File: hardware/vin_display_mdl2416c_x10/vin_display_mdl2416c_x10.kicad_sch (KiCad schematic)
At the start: 34 parts

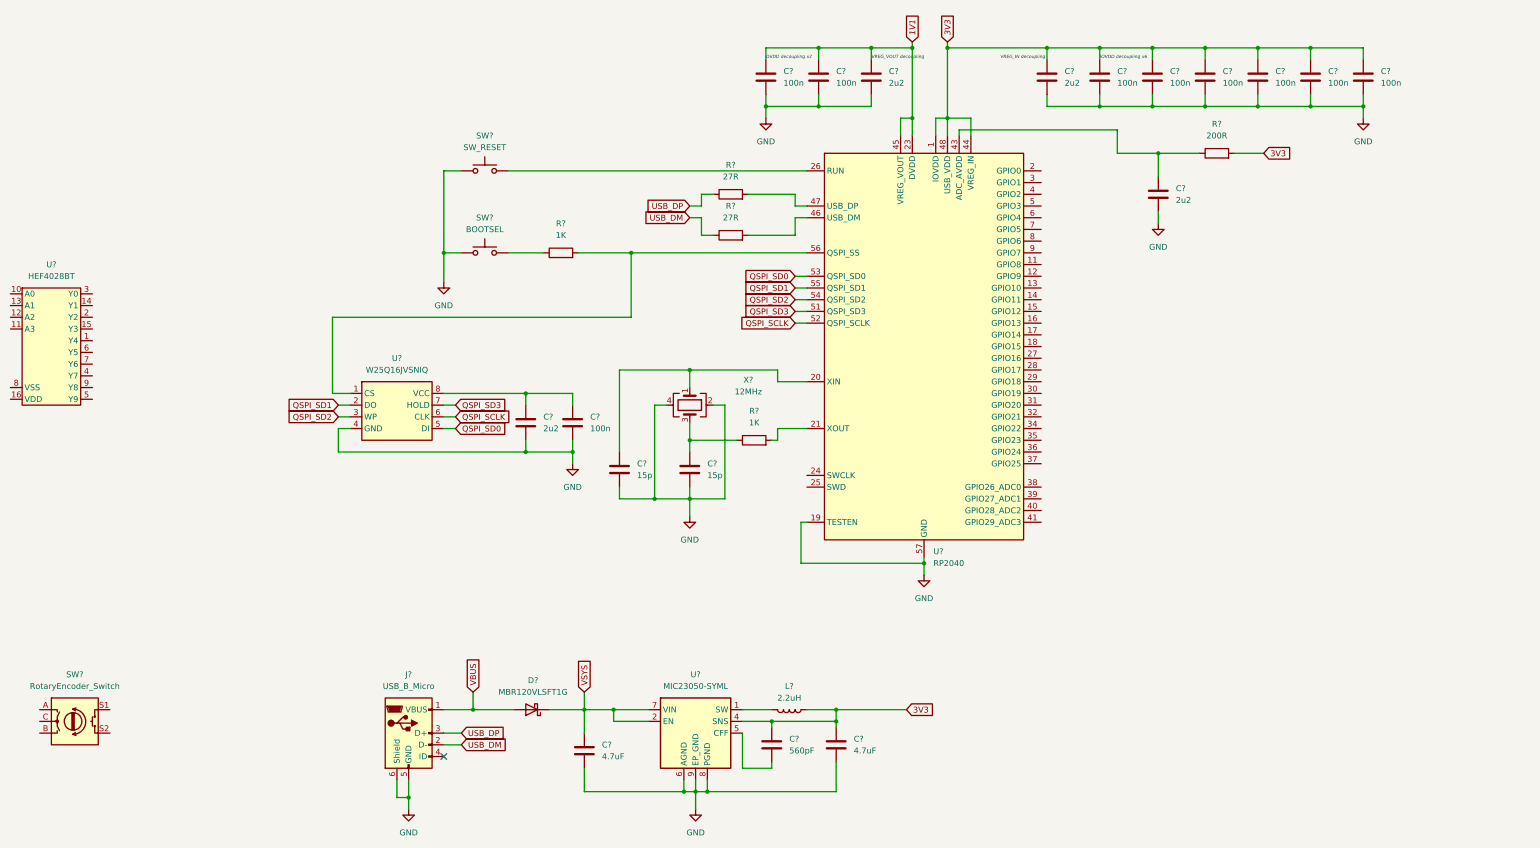
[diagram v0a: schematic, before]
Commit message: complete mdl2416c display schematics
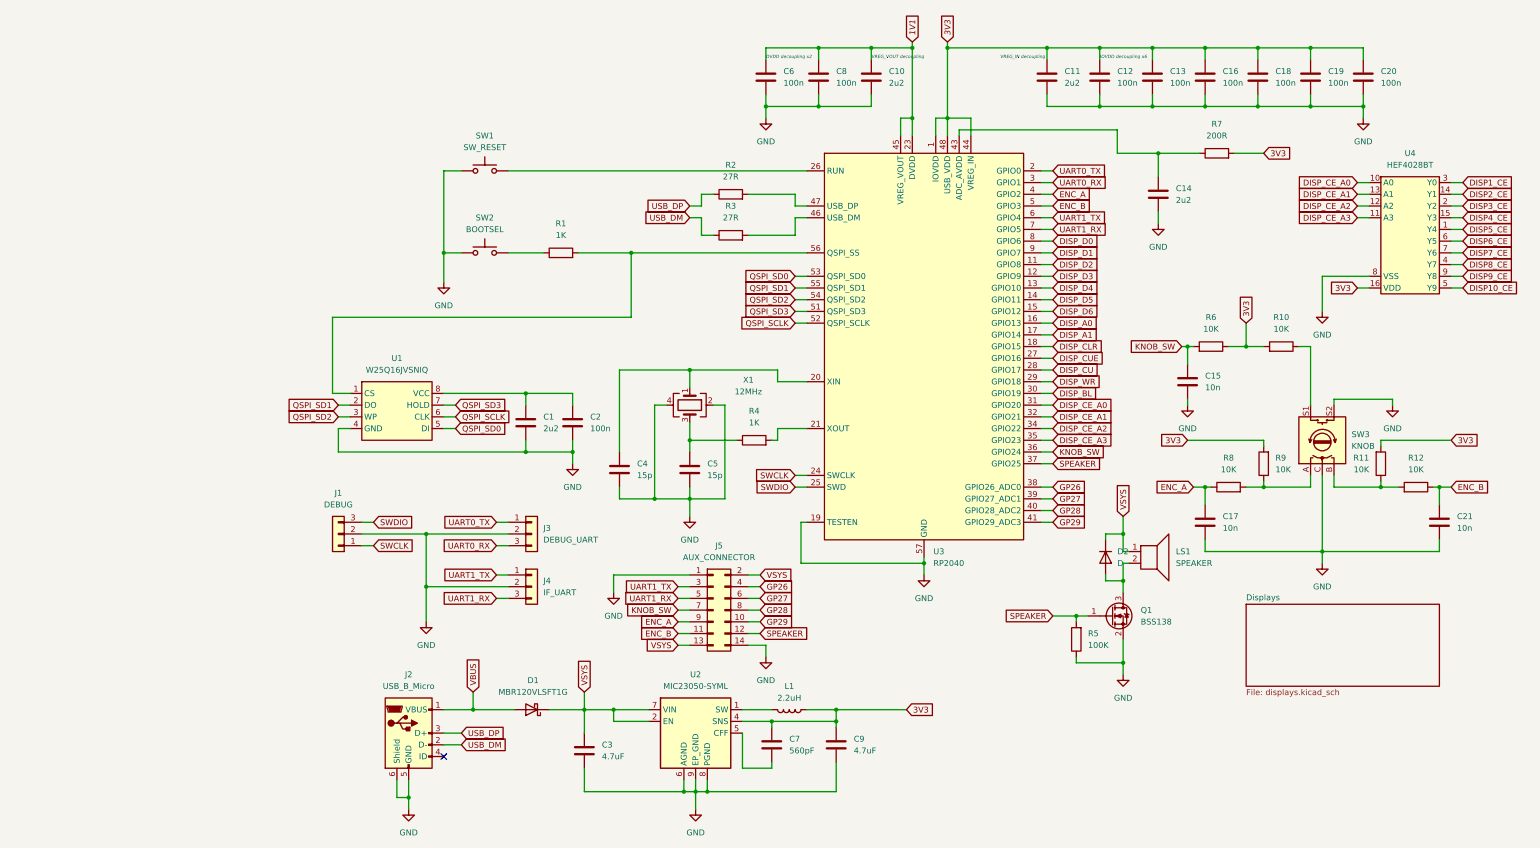
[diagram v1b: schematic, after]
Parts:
- added C15, C17, C21: 10n, symbol Device:C
- added D2: D, symbol Device:D
- added J1: DEBUG, symbol Connector_Generic:Conn_01x03
- added J3: DEBUG_UART, symbol Connector_Generic:Conn_01x03
- added J4: IF_UART, symbol Connector_Generic:Conn_01x03
- added J5: AUX_CONNECTOR, symbol Connector_Generic:Conn_02x07_Odd_Even
- added LS1: SPEAKER, symbol Device:Speaker
- added Q1: BSS138, Package_TO_SOT_SMD:SOT-23, symbol Transistor_FET:BSS138
- added R10, R11, R12, R6, R8, R9: 10K, symbol Device:R
- added R5: 100K, symbol Device:R
- SW3: renamed from SW?; value RotaryEncoder_Switch -> KNOB
- gave numbers to parts that had none: 33
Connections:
- net 3V3: now also U4.16 (VDD), R10.2, R11.2, R6.1, R9.2
- net GND: now also SW3.C, SW3.S2, U4.8 (VSS), C15.2, C17.2, C21.2, J1.2 (Pin_2), J3.2 (Pin_2), J4.2 (Pin_2), J5.1 (Pin_1), J5.14 (Pin_14), Q1.2 (S), R5.1
- net VSYS: now also D2.1 (K), J5.13 (Pin_13), J5.2 (Pin_2), LS1.1
- net DISP5_CE: now reaches U4.1 (Y4)
- net DISP_CE_A0: now reaches U4.10 (A0)
- net DISP_CE_A0: now also U3.31 (GPIO20)
- net DISP_CE_A3: now reaches U4.11 (A3)
- net DISP_CE_A3: now also U3.35 (GPIO23)
- net DISP_CE_A2: now reaches U4.12 (A2)
- net DISP_CE_A2: now also U3.34 (GPIO22)
- net DISP_CE_A1: now reaches U4.13 (A1)
- net DISP_CE_A1: now also U3.32 (GPIO21)
- net DISP2_CE: now reaches U4.14 (Y1)
- net DISP4_CE: now reaches U4.15 (Y3)
- net DISP3_CE: now reaches U4.2 (Y2)
- net DISP1_CE: now reaches U4.3 (Y0)
- net DISP8_CE: now reaches U4.4 (Y7)
- net DISP10_CE: now reaches U4.5 (Y9)
- net DISP6_CE: now reaches U4.6 (Y5)
- net DISP7_CE: now reaches U4.7 (Y6)
- net DISP9_CE: now reaches U4.9 (Y8)
- net DISP_D2: now reaches U3.11 (GPIO8)
- net DISP_D3: now reaches U3.12 (GPIO9)
- net DISP_D4: now reaches U3.13 (GPIO10)
- net DISP_D5: now reaches U3.14 (GPIO11)
- net DISP_D6: now reaches U3.15 (GPIO12)
- net DISP_A0: now reaches U3.16 (GPIO13)
- net DISP_A1: now reaches U3.17 (GPIO14)
- net DISP_CLR: now reaches U3.18 (GPIO15)
- net UART0_TX: now reaches U3.2 (GPIO0)
- net UART0_TX: now also J3.1 (Pin_1)
- net SWCLK: now reaches U3.24 (SWCLK)
- net SWCLK: now also J1.1 (Pin_1)
- net SWDIO: now reaches U3.25 (SWD)
- net SWDIO: now also J1.3 (Pin_3)
- net DISP_CUE: now reaches U3.27 (GPIO16)
- net DISP_CU: now reaches U3.28 (GPIO17)
- net DISP_WR: now reaches U3.29 (GPIO18)
- net UART0_RX: now reaches U3.3 (GPIO1)
- net UART0_RX: now also J3.3 (Pin_3)
- net DISP_BL: now reaches U3.30 (GPIO19)
- net KNOB_SW: now reaches U3.36 (GPIO24)
- net KNOB_SW: now also C15.1, J5.7 (Pin_7), R6.2
- net SPEAKER: now reaches U3.37 (GPIO25)
- net SPEAKER: now also J5.12 (Pin_12), Q1.1 (G), R5.2
- net GP26: now reaches U3.38 (GPIO26_ADC0)
- net GP26: now also J5.4 (Pin_4)
- net GP27: now reaches U3.39 (GPIO27_ADC1)
- net GP27: now also J5.6 (Pin_6)
- net ENC_A: now reaches U3.4 (GPIO2)
- net ENC_A: now also C17.1, J5.9 (Pin_9), R8.1
- net GP28: now reaches U3.40 (GPIO28_ADC2)
- net GP28: now also J5.8 (Pin_8)
- net GP29: now reaches U3.41 (GPIO29_ADC3)
- net GP29: now also J5.10 (Pin_10)
- net ENC_B: now reaches U3.5 (GPIO3)
- net ENC_B: now also C21.1, J5.11 (Pin_11), R12.1
- net UART1_TX: now reaches U3.6 (GPIO4)
- net UART1_TX: now also J4.1 (Pin_1), J5.3 (Pin_3)
- net UART1_RX: now reaches U3.7 (GPIO5)
- net UART1_RX: now also J4.3 (Pin_3), J5.5 (Pin_5)
- net DISP_D0: now reaches U3.8 (GPIO6)
- net DISP_D1: now reaches U3.9 (GPIO7)
- net at SW3.A: now also R8.2, R9.1
- net at SW3.B: now also R11.1, R12.2
- net at SW3.S1: now also R10.1
- new net: D2.2 (A), LS1.2, Q1.3 (D)
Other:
- added sheet Displays (displays.kicad_sch)
- moved on the sheet: SW3, U4

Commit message: assign component footprints; basic pcb layout
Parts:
- C1, C10, C11, C12, C13, C14, C15, C16, C17, C18, C19, C2, C20, C21, C3, C4, C5, C6, C7, C8, C9: footprint (none) -> Capacitor_SMD:C_0603_1608Metric
- D1: value MBR120VLSFT1G -> MBR1020VL; footprint (none) -> Diode_SMD:D_SOD-123F
- D2: footprint (none) -> Diode_SMD:D_SOD-123
- J1, J3, J4: footprint (none) -> Connector_PinHeader_2.54mm:PinHeader_1x03_P2.54mm_Vertical
- J2: footprint (none) -> components:GCT_USB3140
- J5: footprint (none) -> Connector_IDC:IDC-Header_2x07_P2.54mm_Vertical
- L1: footprint (none) -> components:Inductor_0806
- LS1: footprint (none) -> components:BUZZER_CMT-8504
- R1, R10, R11, R12, R2, R3, R4, R5, R6, R7, R8, R9: footprint (none) -> Resistor_SMD:R_0603_1608Metric
- SW1, SW2: footprint (none) -> components:TS18_TACTILE_SWITCH
- SW3: footprint (none) -> components:PEC11H_Encoder
- X1: footprint (none) -> Crystal:Crystal_SMD_Abracon_ABM8AIG-4Pin_3.2x2.5mm

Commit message: work on pcb layout
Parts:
- removed J4: IF_UART, Connector_PinHeader_2.54mm:PinHeader_1x03_P2.54mm_Vertical, symbol Connector_Generic:Conn_01x03
- added J4: Conn_01x04, Connector_PinHeader_2.54mm:PinHeader_1x04_P2.54mm_Vertical, symbol Connector_Generic:Conn_01x04
- U2: footprint Package_DFN_QFN:Micrel_MLF-8-1EP_2x2mm_P0.5mm_EP0.6x1.2mm_ThermalVias -> Package_DFN_QFN:Micrel_MLF-8-1EP_2x2mm_P0.5mm_EP0.6x1.2mm
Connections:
- net 3V3: now also C1.1, C2.1, U1.8 (VCC)
- net GND: now also J4.3 (Pin_3)
- net UART1_RX: now also J4.4 (Pin_4)
- net UART1_TX: now also J4.2 (Pin_2)
- net VSYS: now also J4.1 (Pin_1)
- net USB_D-: now reaches R3.2, U3.46 (USB_DM)
- net USB_D+: now reaches R2.2, U3.47 (USB_DP)
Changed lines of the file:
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@@
+    (stroke (width 0) (type default) (color 0 0 0 0))
+  )
+  (wire (pts (xy 60.96 134.62) (xy 63.5 134.62))
     (stroke (width 0) (type default) (color 0 0 0 0))
   )
@@
     )
   )
+  (global_label "3V3" (shape input) (at 67.31 97.79 90) (fields_autoplaced)
+    (effects (font (size 1.27 1.27)) (justify left))
+    (property "Intersheet References" "${INTERSHEET_REFS}" (id 0) (at 67.2306 91.8693 90)
+      (effects (font (size 1.27 1.27)) (justify left) hide)
+    )
+  )
   (global_label "VBUS" (shape input) (at 55.88 162.56 90) (fields_autoplaced)
     (effects (font (size 1.27 1.27)) (justify left))
@@
     (property "Intersheet References" "${INTERSHEET_REFS}" (id 0) (at 193.0341 59.6106 0)
       (effects (font (size 1.27 1.27)) (justify left) hide)
+    )
+  )
+  (global_label "USB_D-" (shape input) (at 125.73 59.69 180) (fields_autoplaced)
+    (effects (font (size 1.27 1.27)) (justify right))
+    (property "Intersheet References" "${INTERSHEET_REFS}" (id 0) (at 115.6969 59.6106 0)
+      (effects (font (size 1.27 1.27)) (justify right) hide)
     )
   )
@@
     (effects (font (size 1.27 1.27)) (justify right))
     (property "Intersheet References" "${INTERSHEET_REFS}" (id 0) (at 114.2455 72.4694 0)
+      (effects (font (size 1.27 1.27)) (justify right) hide)
+    )
+  )
+  (global_label "USB_D+" (shape input) (at 125.73 57.15 180) (fields_autoplaced)
+    (effects (font (size 1.27 1.27)) (justify right))
+    (property "Intersheet References" "${INTERSHEET_REFS}" (id 0) (at 115.6969 57.0706 0)
+      (effects (font (size 1.27 1.27)) (justify right) hide)
+    )
+  )
+  (global_label "VSYS" (shape input) (at 60.96 134.62 180) (fields_autoplaced)
+    (effects (font (size 1.27 1.27)) (justify right))
+    (property "Intersheet References" "${INTERSHEET_REFS}" (id 0) (at 53.9507 134.5406 0)
       (effects (font (size 1.27 1.27)) (justify right) hide)
     )
@@
     )
     (property "Datasheet" "~" (id 3) (at 26.67 128.27 0)
-      (effects (font (size 1.27 1.27)) hide)
-    )
-    (pin "1")
-    (pin "2")
-    (pin "3")
-  )
-  (symbol (lib_id "Connector_Generic:Conn_01x03") (at 68.58 139.7 0) (unit 1)
-    (in_bom yes) (on_board yes) (fields_autoplaced)
-    (property "Reference" "J4" (id 0) (at 71.12 138.4299 0)
-      (effects (font (size 1.27 1.27)) (justify left))
-    )
-    (property "Value" "IF_UART" (id 1) (at 71.12 140.9699 0)
-      (effects (font (size 1.27 1.27)) (justify left))
-    )
-    (property "Footprint" "Connector_PinHeader_2.54mm:PinHeader_1x03_P2.54mm_Vertical" (id 2) (at 68.58 139.7 0)
-      (effects (font (size 1.27 1.27)) hide)
-    )
-    (property "Datasheet" "~" (id 3) (at 68.58 139.7 0)
       (effects (font (size 1.27 1.27)) hide)
     )
@@
     (pin "2")
   )
+  (symbol (lib_id "Connector_Generic:Conn_01x04") (at 68.58 137.16 0) (unit 1)
+    (in_bom yes) (on_board yes) (fields_autoplaced)
+    (property "Reference" "J4" (id 0) (at 71.12 137.1599 0)
+      (effects (font (size 1.27 1.27)) (justify left))
+    )
+    (property "Value" "Conn_01x04" (id 1) (at 71.12 139.6999 0)
+      (effects (font (size 1.27 1.27)) (justify left))
+    )
+    (property "Footprint" "Connector_PinHeader_2.54mm:PinHeader_1x04_P2.54mm_Vertical" (id 2) (at 68.58 137.16 0)
+      (effects (font (size 1.27 1.27)) hide)
+    )
+    (property "Datasheet" "~" (id 3) (at 68.58 137.16 0)
+      (effects (font (size 1.27 1.27)) hide)
+    )
+    (pin "1")
+    (pin "2")
+    (pin "3")
+    (pin "4")
+  )
   (symbol (lib_id "Device:R") (at 111.76 54.61 90) (unit 1)
     (in_bom yes) (on_board yes) (fields_autoplaced)
@@
     (property "Reference" "U2" (id 0) (at 104.14 158.75 0))
     (property "Value" "MIC23050-SYML" (id 1) (at 104.14 161.29 0))
-    (property "Footprint" "Package_DFN_QFN:Micrel_MLF-8-1EP_2x2mm_P0.5mm_EP0.6x1.2mm_ThermalVias" (id 2) (at 109.22 170.18 0)
+    (property "Footprint" "Package_DFN_QFN:Micrel_MLF-8-1EP_2x2mm_P0.5mm_EP0.6x1.2mm" (id 2) (at 109.22 170.18 0)
       (effects (font (size 1.27 1.27)) (justify left) hide)
     )
@@
       (reference "J3") (unit 1) (value "DEBUG_UART") (footprint "Connector_PinHeader_2.54mm:PinHeader_1x03_P2.54mm_Vertical")
     )
-    (path "/52948f66-709e-42ba-95a6-a598f591e63a"
-      (reference "J4") (unit 1) (value "IF_UART") (footprint "Connector_PinHeader_2.54mm:PinHeader_1x03_P2.54mm_Vertical")
+    (path "/83b99386-65f3-4d5f-ace0-dfc7848335c3"
+      (reference "J4") (unit 1) (value "Conn_01x04") (footprint "Connector_PinHeader_2.54mm:PinHeader_1x04_P2.54mm_Vertical")
     )
     (path "/24dea3f5-faa1-4f14-a163-ea0dcc26d440"
@@
     )
     (path "/fc845537-7277-43cf-9d22-ef1876c41284"
-      (reference "U2") (unit 1) (value "MIC23050-SYML") (footprint "Package_DFN_QFN:Micrel_MLF-8-1EP_2x2mm_P0.5mm_EP0.6x1.2mm_ThermalVias")
+      (reference "U2") (unit 1) (value "MIC23050-SYML") (footprint "Package_DFN_QFN:Micrel_MLF-8-1EP_2x2mm_P0.5mm_EP0.6x1.2mm")
     )
     (path "/73b74445-0b4c-42ed-8ac5-ea72e30c4bc1"

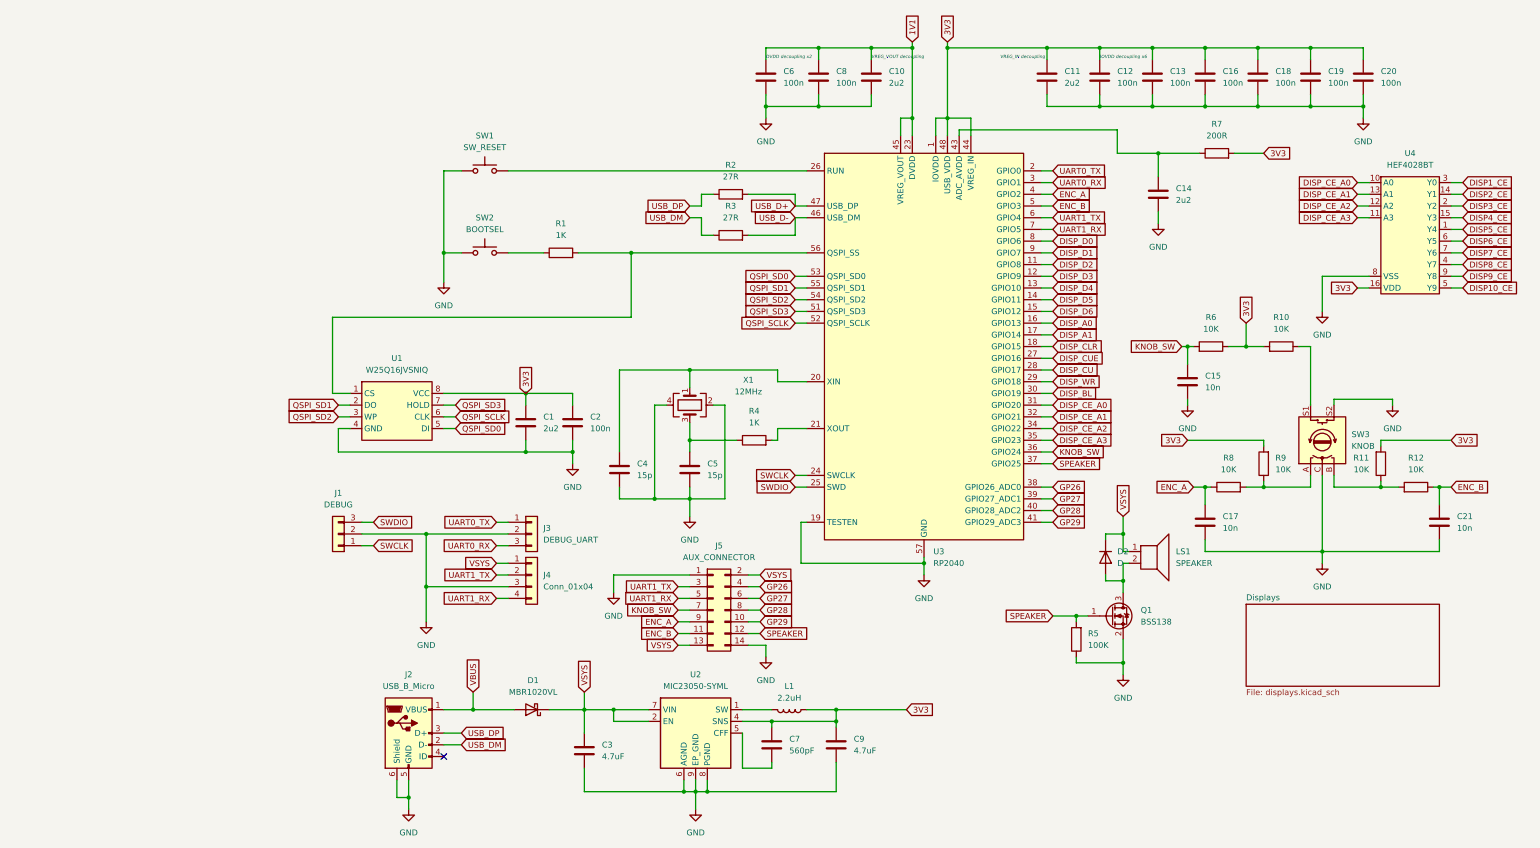
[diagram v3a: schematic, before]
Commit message: mdl2416c_x10 pcb routed
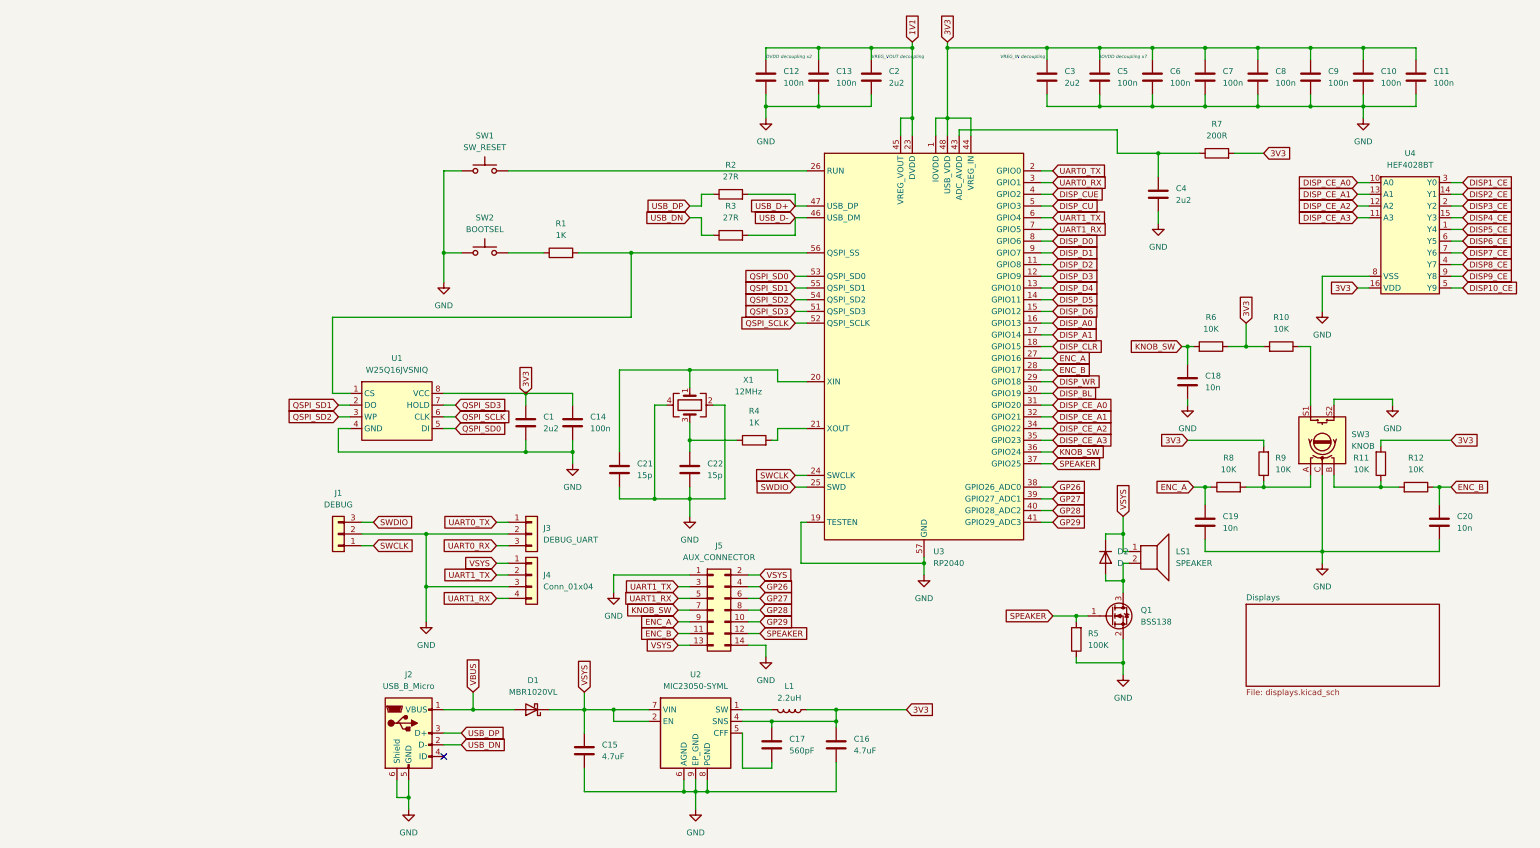
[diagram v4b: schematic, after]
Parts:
- added C11: 100n, Capacitor_SMD:C_0603_1608Metric, symbol Device:C
- renumbered C20 to C10, C6 to C12, C8 to C13, C2 to C14, C3 to C15, C9 to C16, C7 to C17, C15 to C18, C17 to C19, C10 to C2, C21 to C20, C4 to C21, C5 to C22, C11 to C3, C14 to C4, C12 to C5, C13 to C6, C16 to C7, C18 to C8, C19 to C9
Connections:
- net 3V3: now also C11.1
- net DISP_CU: now also U3.5 (GPIO3); no longer U3.28 (GPIO17)
- net DISP_CUE: now also U3.4 (GPIO2); no longer U3.27 (GPIO16)
- net ENC_A: now also U3.27 (GPIO16); no longer U3.4 (GPIO2)
- net ENC_B: now also U3.28 (GPIO17); no longer U3.5 (GPIO3)
- net GND: now also C11.2
- net USB_DM renamed USB_DN
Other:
- note added: "IOVDD decoupling x7"
- note removed: "IOVDD decoupling x6"
